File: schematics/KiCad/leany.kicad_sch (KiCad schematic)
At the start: 40 parts, among them J1 SWD, J2 SSD1306, J3 USB_C, Q1 DMG6601LVT-7, SW2 ZERO_BTN, SW3 HOLD_BTN, SW4 BOOTMODE_SW, U1 STM32F103C8Tx, U2 AP2112K-3.3, U3 LSM6DSO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

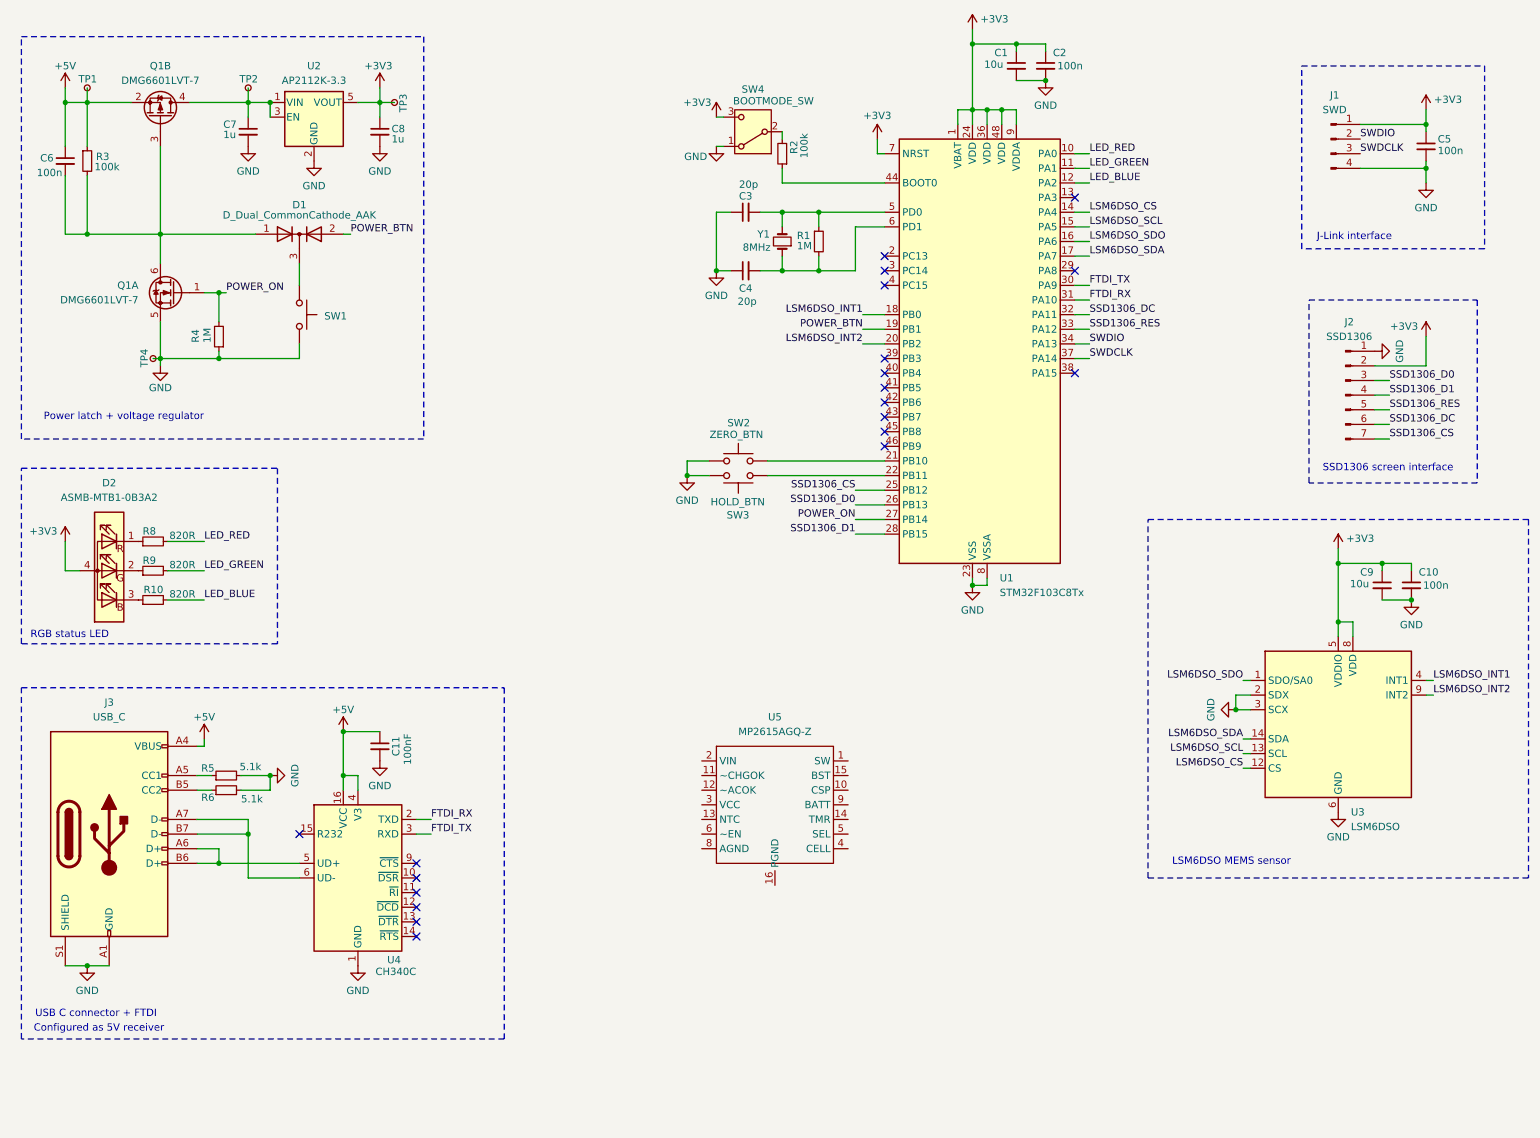
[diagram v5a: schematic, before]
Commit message: move power-management related components to their own sheet
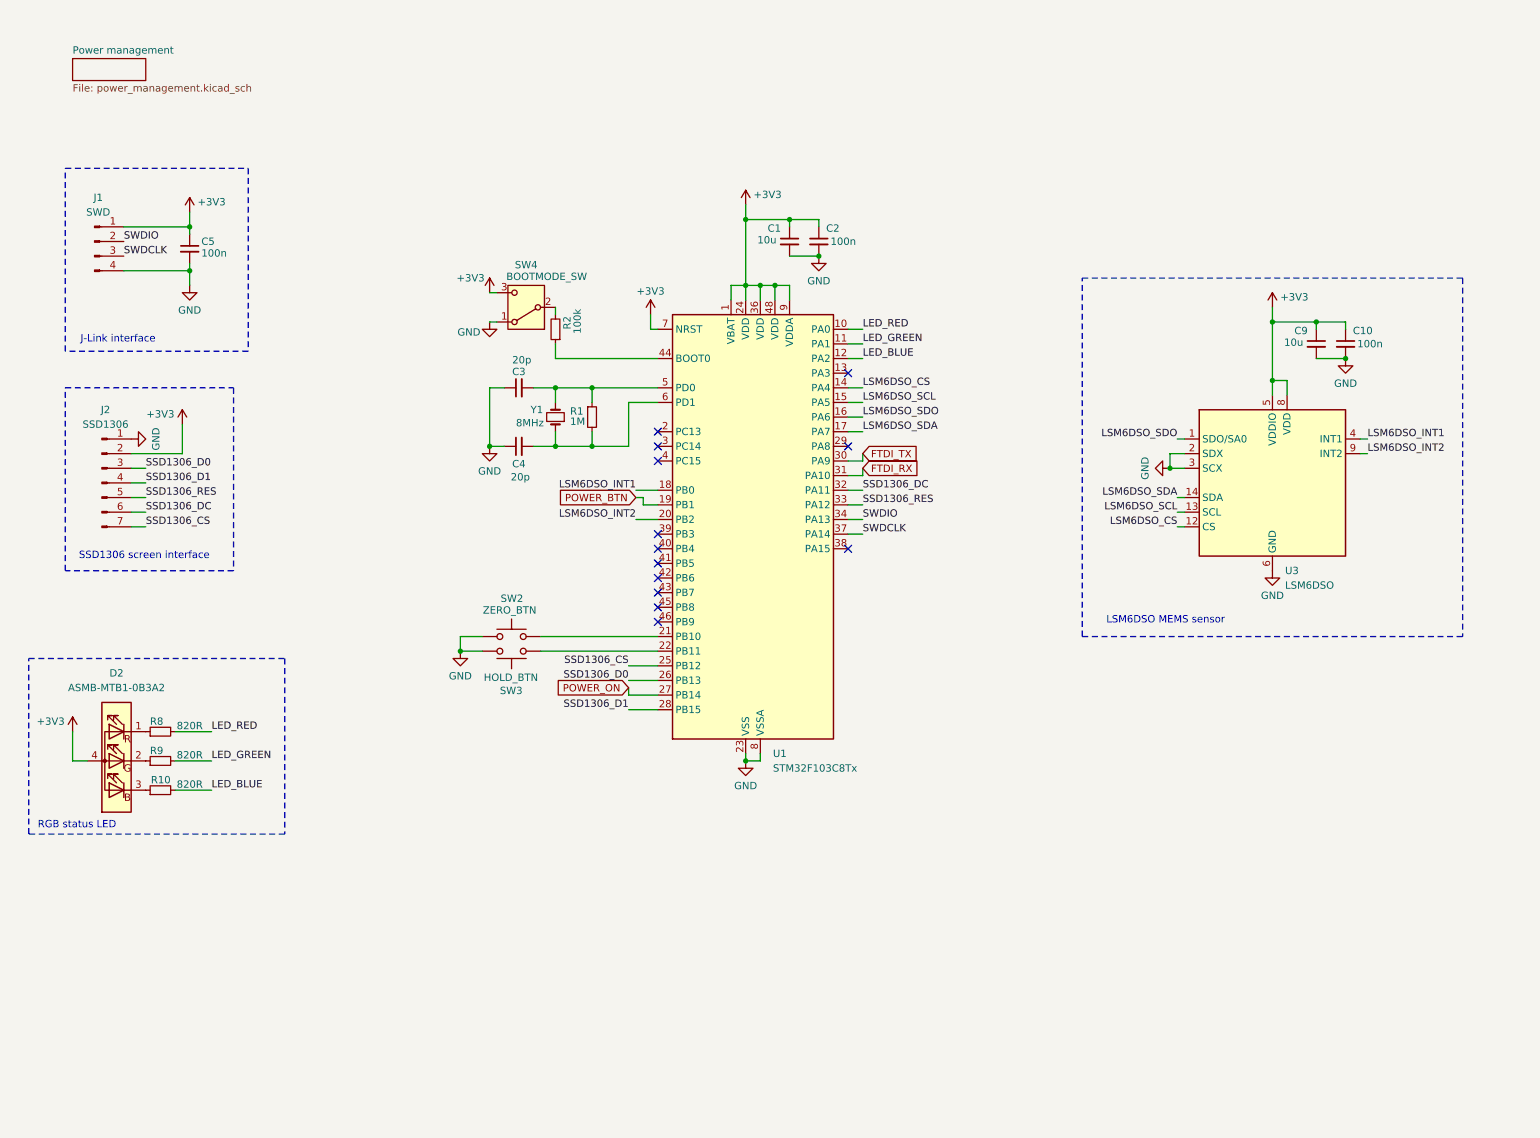
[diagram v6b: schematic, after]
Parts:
- removed C11: 100nF, Capacitor_SMD:C_0201_0603Metric, symbol Device:C_Small
- removed C6: 100n, Capacitor_SMD:C_0201_0603Metric, symbol Device:C_Small
- removed C7, C8: 1u, Capacitor_SMD:C_0201_0603Metric, symbol Device:C_Small
- removed D1: D_Dual_CommonCathode_AAK, symbol Device:D_Dual_CommonCathode_AAK
- removed J3: USB_C, Connector_USB:USB_C_Receptacle_GCT_USB4105-xx-A_16P_TopMnt_Horizontal, symbol Connector:USB_C_Receptacle_USB2.0_14P
- removed Q1: DMG6601LVT-7, Package_TO_SOT_SMD:TSOT-23-6, symbol leany-symbols:DMG6601LVT-7
- removed R3: 100k, Resistor_SMD:R_0603_1608Metric, symbol Device:R_Small
- removed R4: 1M, Resistor_SMD:R_0603_1608Metric, symbol Device:R_Small
- removed R5, R6: 5.1k, Resistor_SMD:R_0603_1608Metric, symbol Device:R_Small
- removed SW1: ~, symbol Switch:SW_Push
- removed TP1: 5V, TestPoint:TestPoint_Pad_1.0x1.0mm, symbol Connector:TestPoint_Small
- removed TP2: Vin, TestPoint:TestPoint_Pad_1.0x1.0mm, symbol Connector:TestPoint_Small
- removed TP3: 3.3V, TestPoint:TestPoint_Pad_1.0x1.0mm, symbol Connector:TestPoint_Small
- removed TP4: GND, TestPoint:TestPoint_Pad_1.0x1.0mm, symbol Connector:TestPoint_Small
- removed U2: AP2112K-3.3, Package_TO_SOT_SMD:SOT-23-5, symbol Regulator_Linear:AP2112K-3.3
- removed U4: CH340C, Package_SO:SOIC-16_3.9x9.9mm_P1.27mm, symbol Interface_USB:CH340C
- removed U5: MP2615AGQ-Z, symbol leany-symbols:MP2615AGQ-Z
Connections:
- no-connect marks 20 -> 13
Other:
- added sheet Power management (power_management.kicad_sch)
- note removed: "Configured as 5V receiver"
- note removed: "Power latch + voltage regulator"
- note removed: "USB C connector + FTDI"
- moved on the sheet: C1, C10, C2, C3, C4, C5, C9, D2, J1, J2, R1, R10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

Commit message: move FTDI chip back to main page
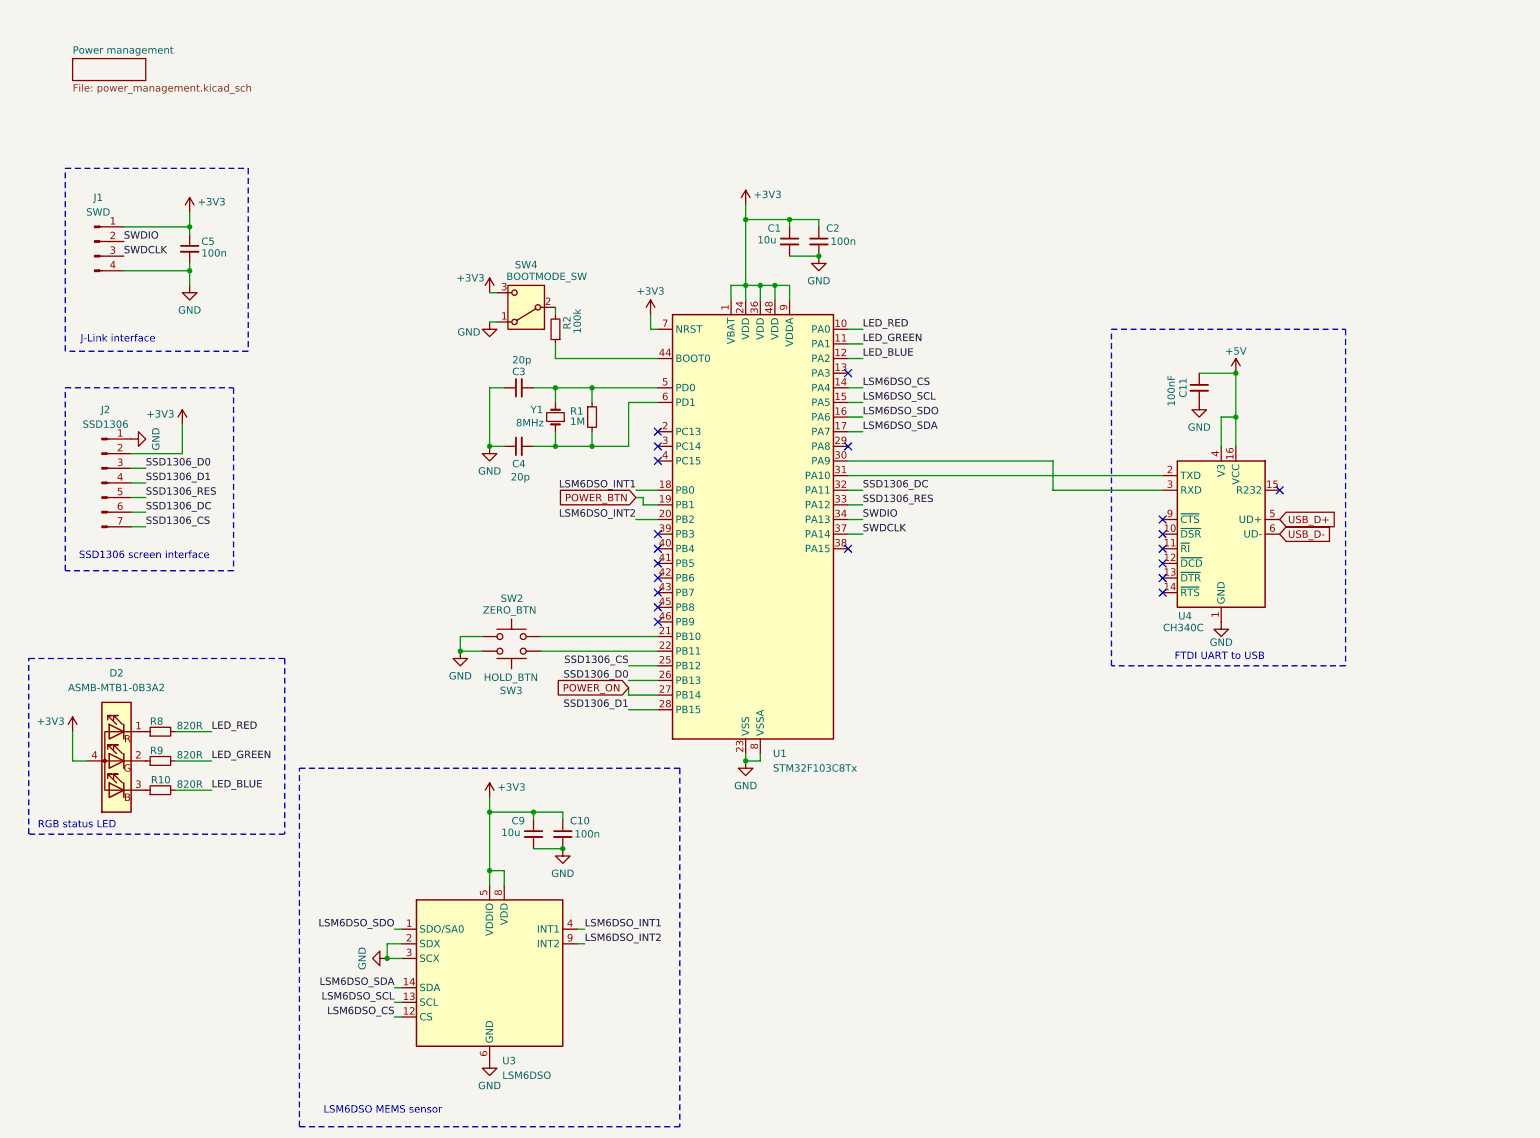
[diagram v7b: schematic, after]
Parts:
- added C11: 100nF, Capacitor_SMD:C_0201_0603Metric, symbol Device:C_Small
- added U4: CH340C, Package_SO:SOIC-16_3.9x9.9mm_P1.27mm, symbol Interface_USB:CH340C
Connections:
- net GND: now also C11.2, U4.1 (GND)
- net FTDI_RX: no longer names the net of U1.31 (PA10)
- net FTDI_RX: now also U4.2 (TXD)
- net FTDI_TX: no longer names the net of U1.30 (PA9)
- net FTDI_TX: now also U4.3 (RXD)
- new net +5V: C11.1, U4.16 (VCC), U4.4 (V3)
- new net USB_D+: U4.5 (UD+)
- new net USB_D-: U4.6 (UD-)
- no-connect marks 13 -> 20
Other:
- note added: "FTDI UART to USB"
- moved on the sheet: C10, C9, U3

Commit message: reorganise symbols
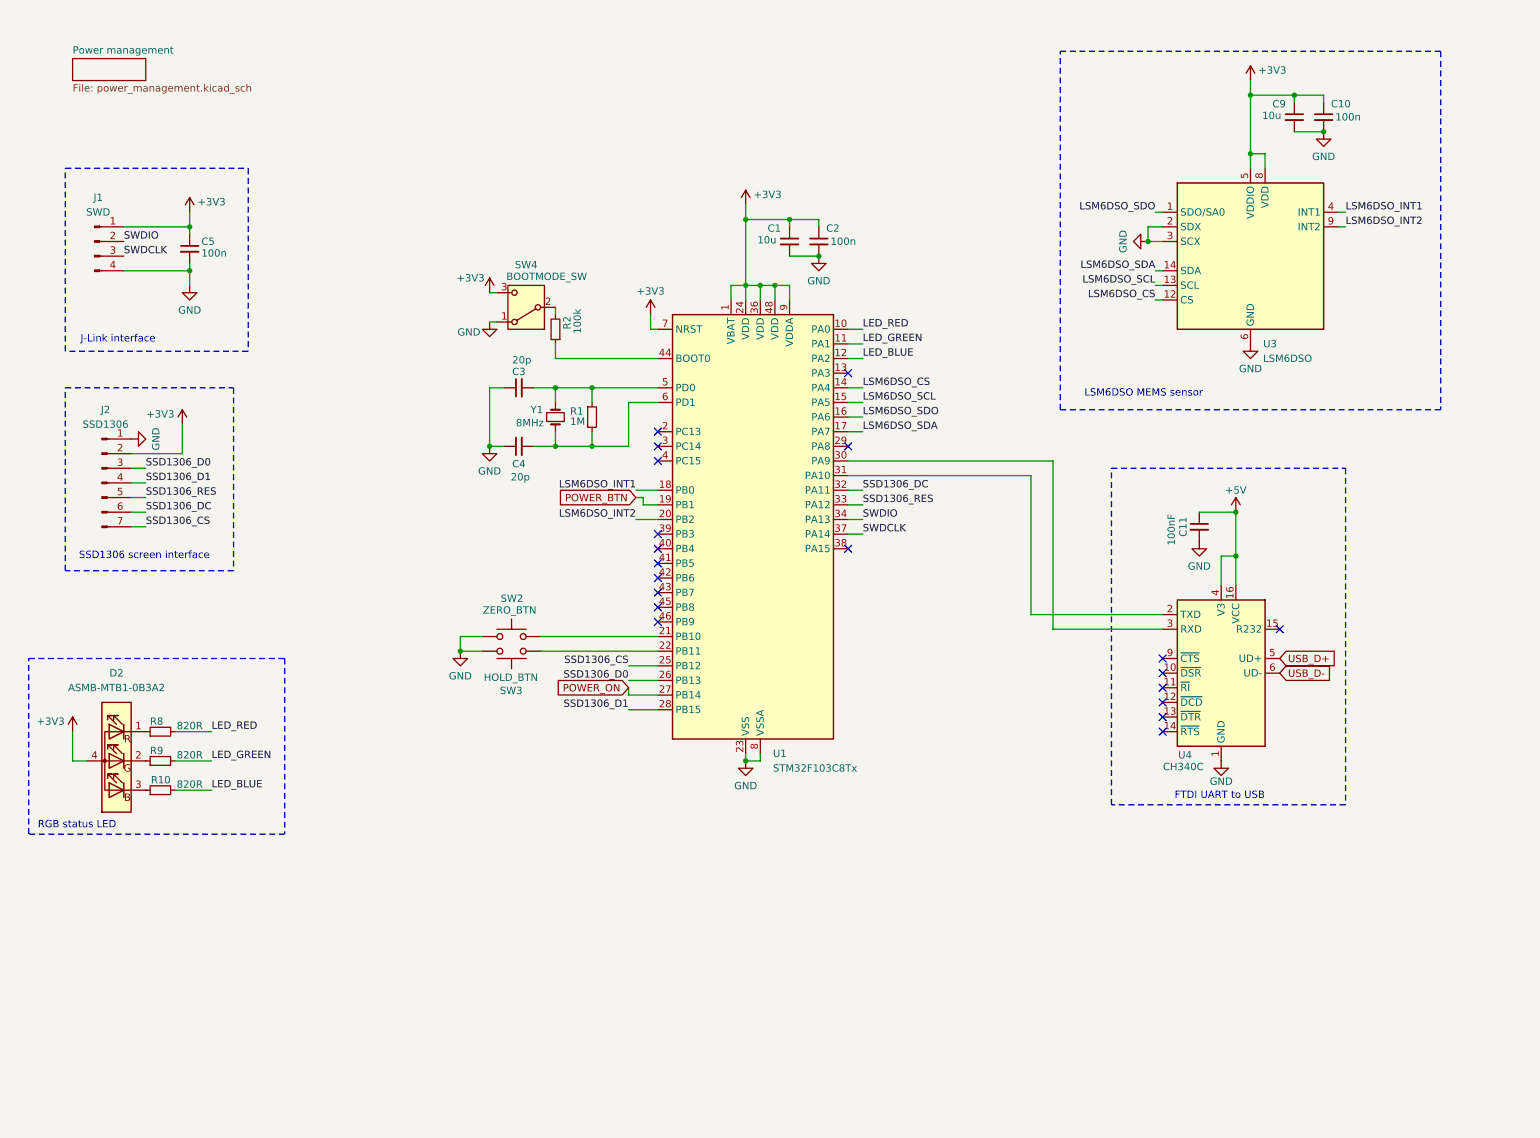
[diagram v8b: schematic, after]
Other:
- moved on the sheet: C10, C11, C9, U3, U4
